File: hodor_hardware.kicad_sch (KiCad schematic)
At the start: 0 parts

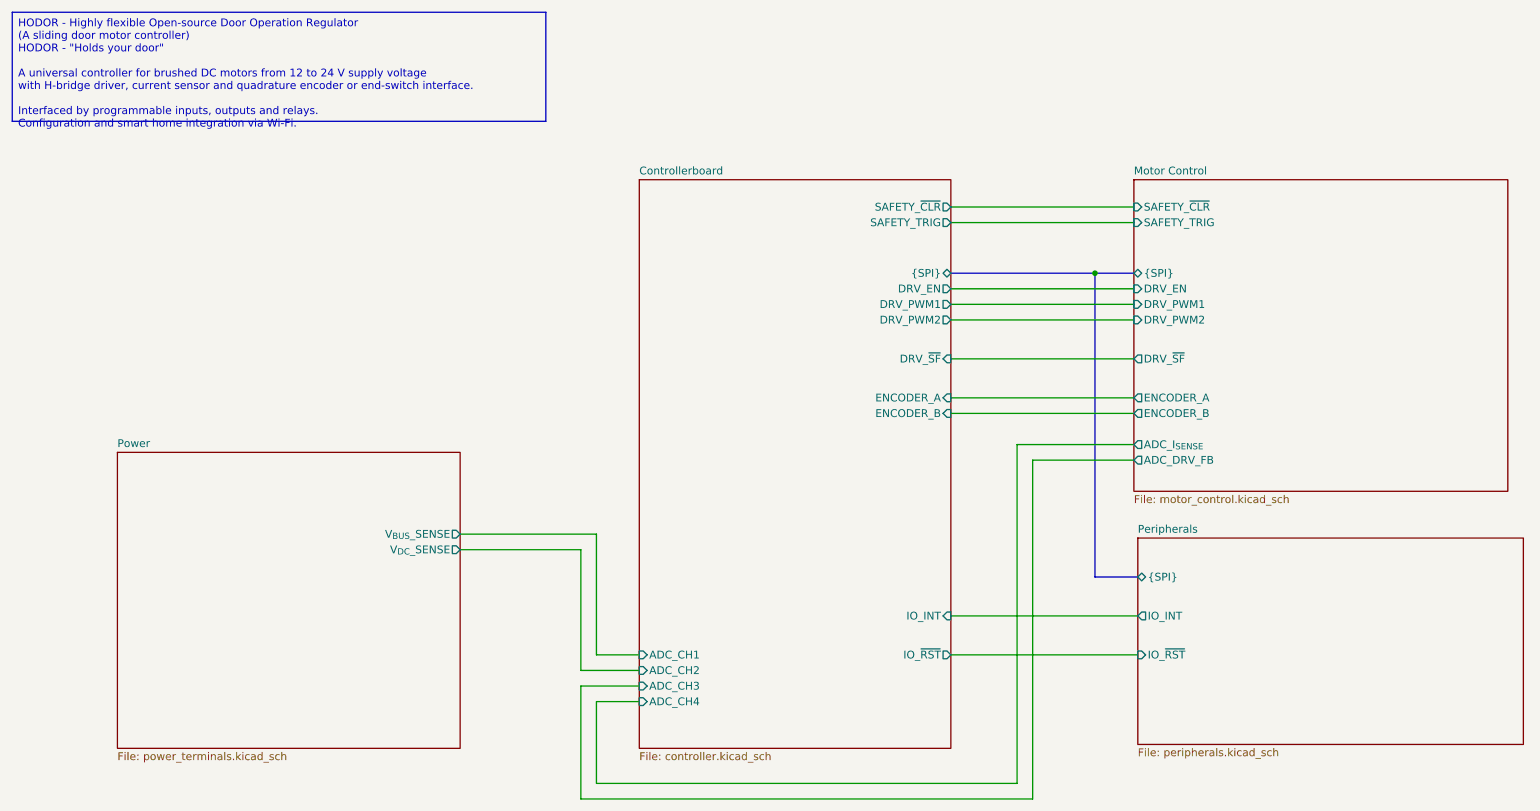
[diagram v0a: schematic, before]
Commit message: Simplified design (Old version switched to hodor-max)
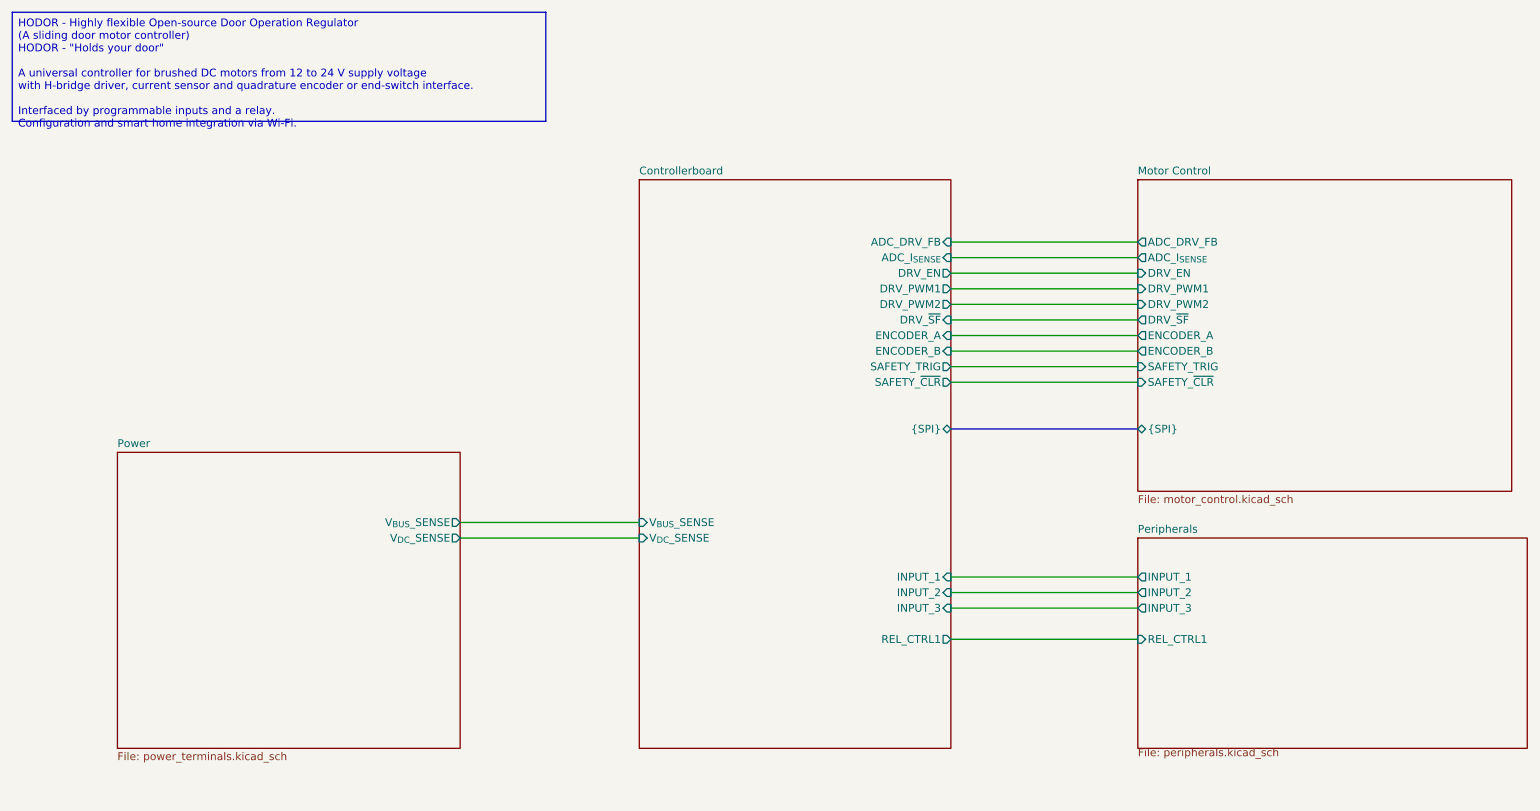
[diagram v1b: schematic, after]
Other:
- sheet Controllerboard ports: added ADC_DRV_FB, ADC_I_{SENSE}, INPUT_1, INPUT_2, INPUT_3, REL_CTRL1, V_{BUS}_SENSE, V_{DC}_SENSE; removed ADC_CH1, ADC_CH2, ADC_CH3, ADC_CH4, IO_INT, IO_~{RST}
- sheet Peripherals ports: added INPUT_1, INPUT_2, INPUT_3, REL_CTRL1; removed IO_INT, IO_~{RST}, {SPI}
